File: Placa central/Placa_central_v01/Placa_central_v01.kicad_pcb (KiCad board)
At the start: 2 copper layers, 36 parts, among them J1 Conn_8.4V_PlacaAlimentação, J16 Conn_01x01_Motor1PonteHPCB, J2 Conn_01x02_ArduinoTxRx, J26 Conn_02x08_Odd_Even, J27 Conn_01x01_Motor2PonteHPCB, J28 Conn_01x01_Motor1PCBMotor, J29 Conn_01x01_Motor2PCBMotor, J3 Conn_01x01_ArduinoReset, J37 Conn_01x01_8.4VPonteH, J38 Conn_01x01_5VPonteH, J39 Conn_01x01_GNDPonteH, J4 Conn_GND_PlacaAlimentação, J40 Conn_01x01_Motor1PWM, J41 Conn_01x01_Motor1Dir1, J42 Conn_01x01_Motor1Dir2, J43 Conn_01x01_Motor2Dir1, J44 Conn_01x01_Motor2Dir2, J45 Conn_01x01_Motor2PWM, J48 Conn_01x01_5VEncoderEsq, J49 Conn_01x01_OutputEncoderEsq, J50 Conn_01x01_GNDEncoderEsq, J51 Conn_01x01_5VEncoderDir, J52 Conn_01x01_OutputEncoderDir, J53 Conn_01x01_GNDEncoderDir, SW3 SW_comando1

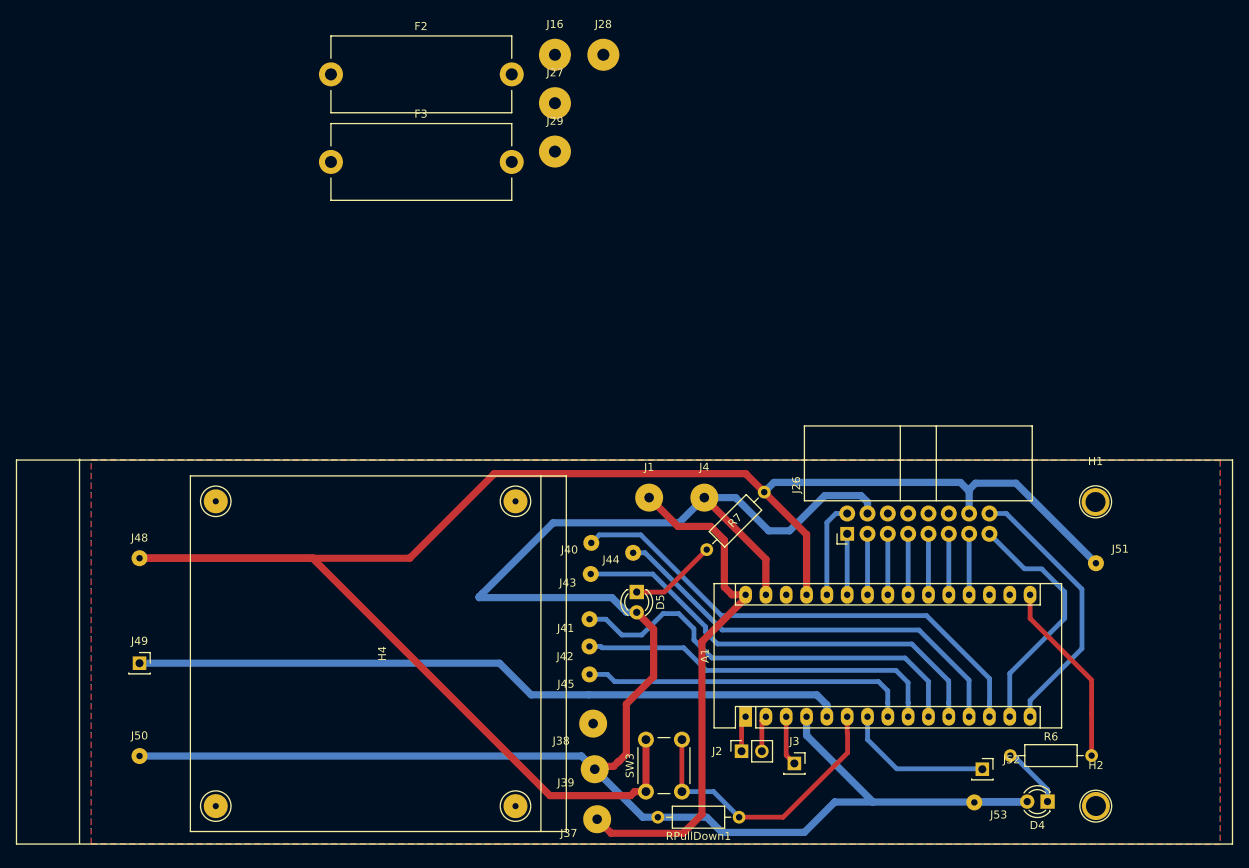
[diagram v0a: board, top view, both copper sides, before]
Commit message: Correção nas pcbs
Nome da placa de encoder desinvertido
Trilhas laterais de GND da placa central mais espaçadas nos cantos
Nome da equipe colocado na placa central
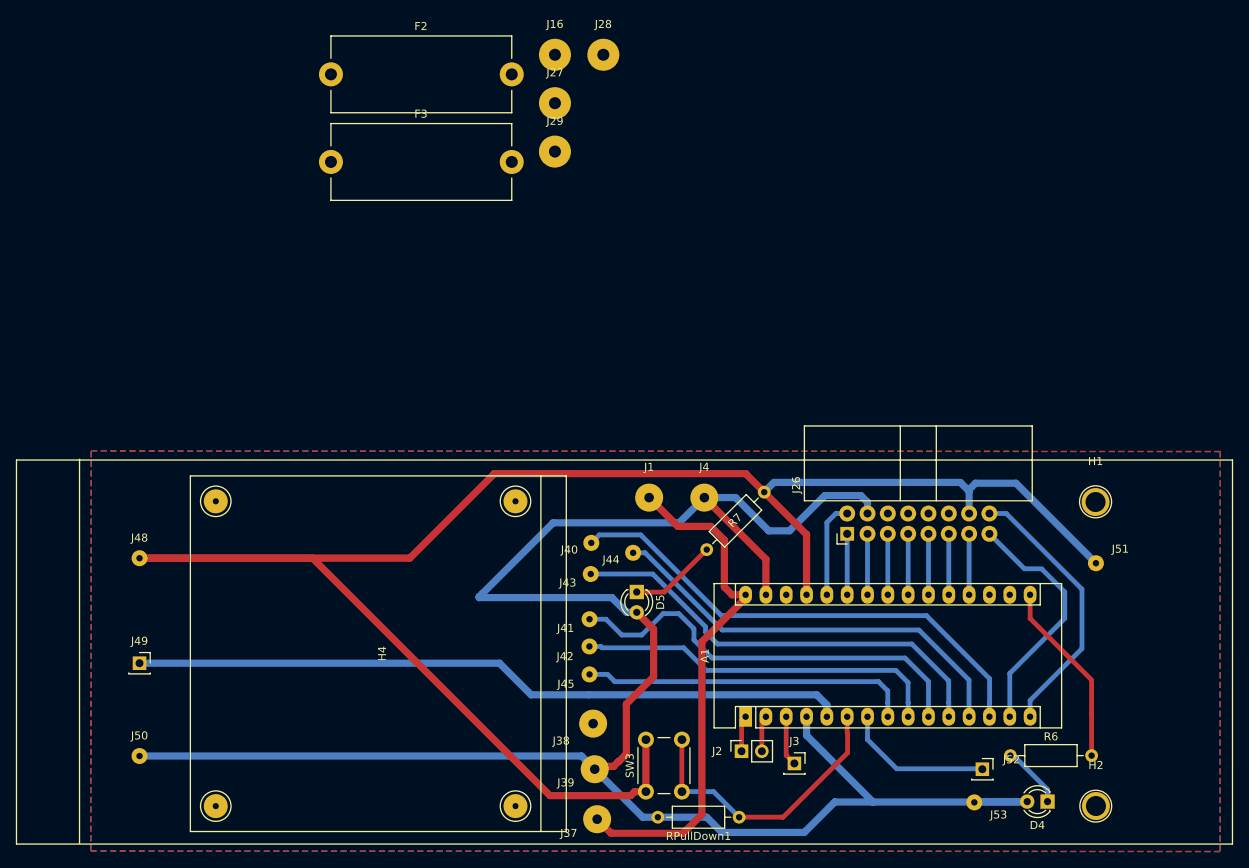
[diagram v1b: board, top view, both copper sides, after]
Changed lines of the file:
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@@
-(kicad_pcb (version 20171130) (host pcbnew 5.1.4-e60b266~84~ubuntu18.04.1)
+(kicad_pcb (version 20171130) (host pcbnew "(5.1.2)-2")
   (general
     (thickness 1.6)
@@
     (visible_elements 7FFFFFFF)
     (pcbplotparams
-      (layerselection 0x000c0_7ffffffe)
+      (layerselection 0x00000_7fffffff)
       (usegerberextensions false)
       (usegerberattributes false)
@@
       (hpglpenspeed 20)
       (hpglpendiameter 15.000000)
-      (psnegative false)
+      (psnegative true)
       (psa4output false)
       (plotreference true)
@@
     (polygon
       (pts
-        (xy 33.95 122.547) (xy 175.1 122.65) (xy 175.1 170.65) (xy 33.95 170.553)
+        (xy 33.95 121.4485) (xy 175.1 121.5515) (xy 175.075 171.5485) (xy 33.925 171.4515)
       )
     )
@@
     (polygon
       (pts
-        (xy 33.95 122.6) (xy 175.1 122.65) (xy 175.1 170.65) (xy 33.95 170.6)
+        (xy 33.95 121.475) (xy 175.1 121.525) (xy 175.075 171.525) (xy 33.925 171.475)
       )
     )

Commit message: Commit complementar ao anterior
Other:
- board text added: "S.L. - ERUS - Pl. CENTRAL"
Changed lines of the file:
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@@
   (general
     (thickness 1.6)
-    (drawings 7)
+    (drawings 9)
     (tracks 190)
     (zones 0)
@@
     (visible_elements 7FFFFFFF)
     (pcbplotparams
-      (layerselection 0x00000_7fffffff)
+      (layerselection 0x00000_fffffffe)
       (usegerberextensions false)
       (usegerberattributes false)
@@
     (pad 1 thru_hole circle (at 0 0) (size 3.5 3.5) (drill 2.49936) (layers *.Cu *.Mask))
   )
+  (gr_text "S.L. - ERUS - Pl. CENTRAL" (at 170.5 147 90) (layer B.Cu)
+    (effects (font (size 1.5 1.5) (thickness 0.375)) (justify mirror))
+  )
+  (gr_text "S.L. - ERUS - Pl. CENTRAL" (at 170.5 147.5 90) (layer F.Cu)
+    (effects (font (size 1.5 1.5) (thickness 0.375)))
+  )
   (gr_line (start 32.5 122.5) (end 32.5 170.5) (layer F.SilkS) (width 0.12))

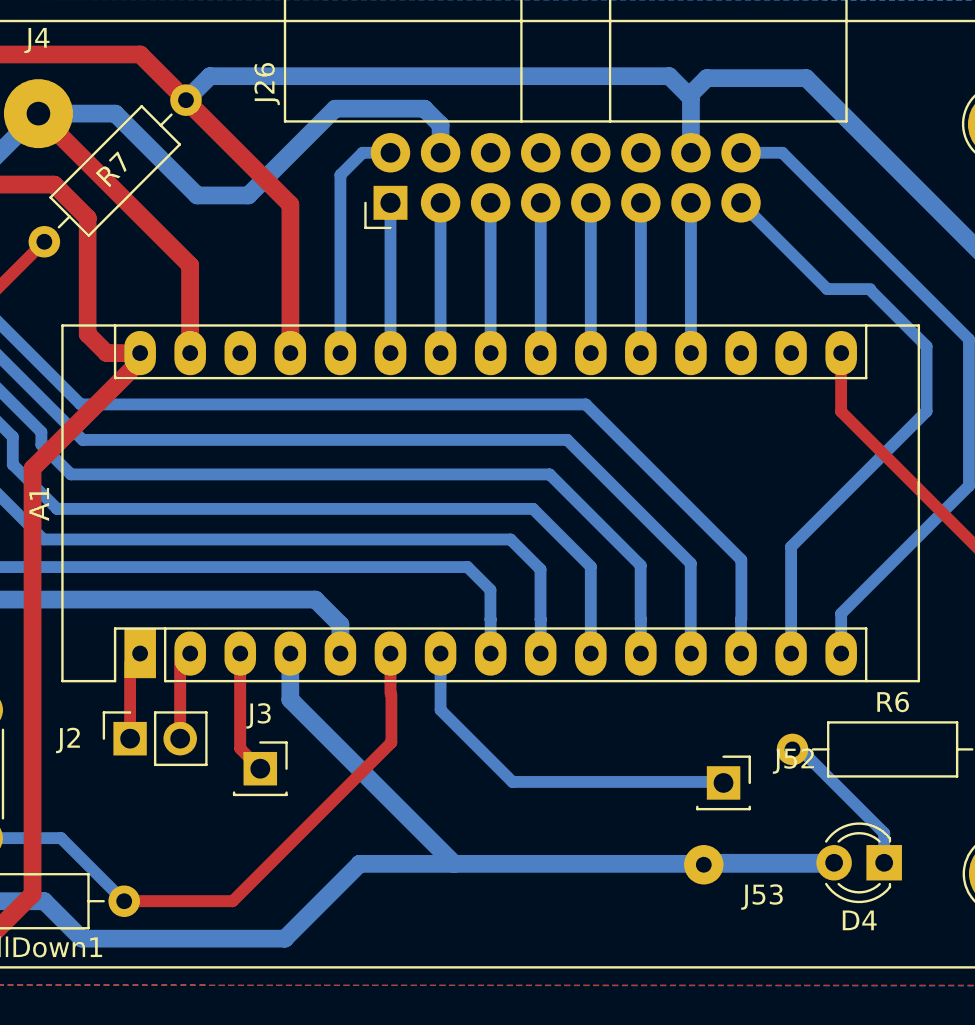
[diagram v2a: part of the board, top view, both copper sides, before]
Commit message: Mudancas criticas na PCB Central, ainda ha pendencias
Foi trocado o pino do botao pelo pino do encoder. Os encoders devem estar obrigatoriamente nos pinos D2 e D3:
Encoder2 para o pino 6 (D3)
Botao1 para o pino 7 (D4);
Aumentadas as dimensoes dos pads conectores do arduino, para mais seguranca ao furar;
Pads do conector modificados para melhor seguranca ao furar;
Clearance da malha de ground aumentada de 0.5 para 0.7
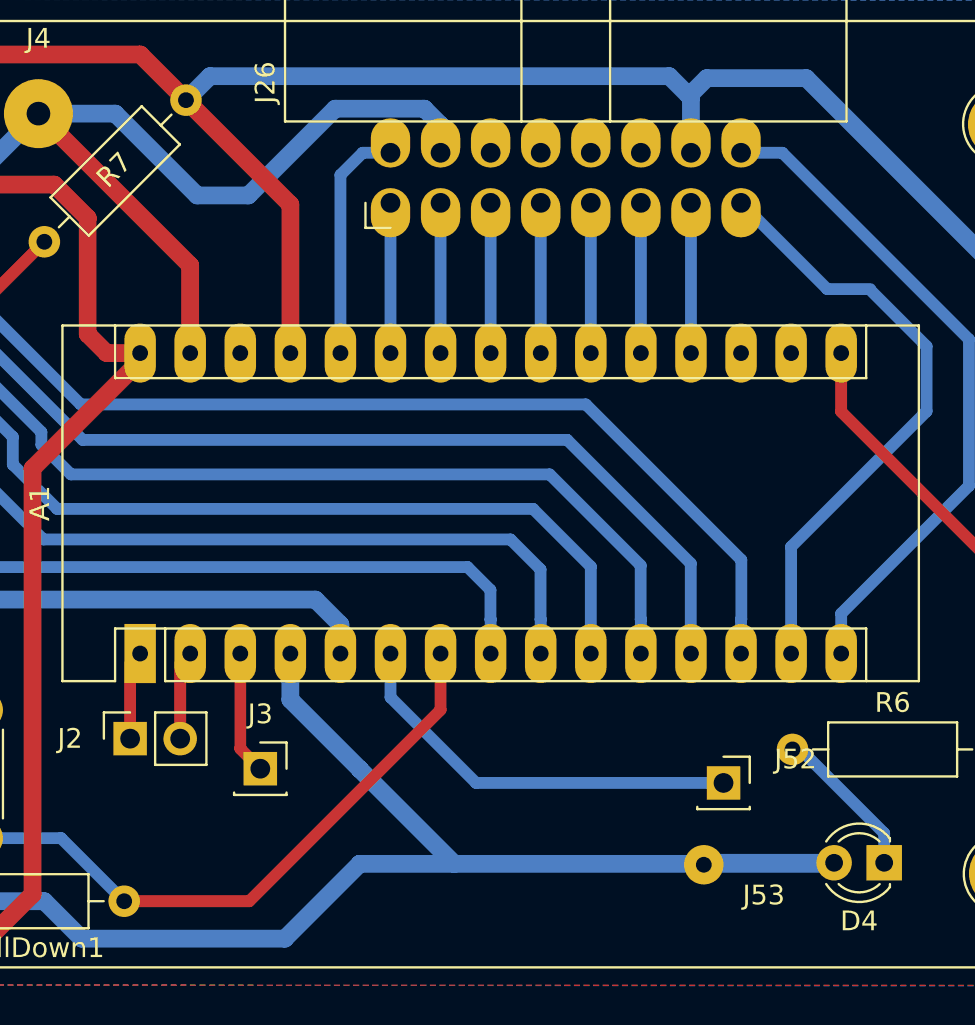
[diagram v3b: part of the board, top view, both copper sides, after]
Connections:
- A1 pad 6: Botao1 -> Encoder2
- A1 pad 7: Encoder2 -> Botao1
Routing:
- net Encoder2: track 18.7 -> 21.2 mm
- net Botao1: track 36.7 -> 37.9 mm

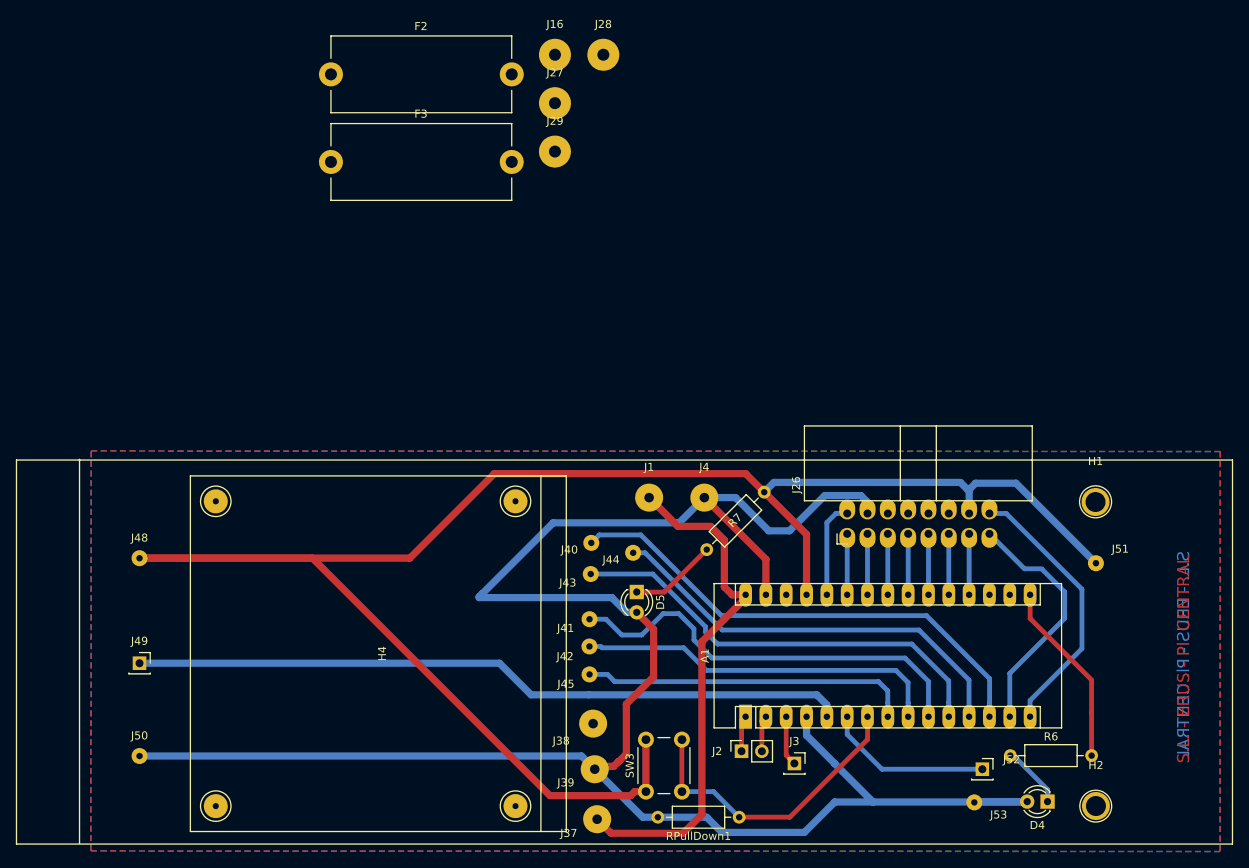
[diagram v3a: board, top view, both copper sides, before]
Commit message: Acertada as placas e os pdfs
Acertada as placas centrais, de alimentação e de conector.
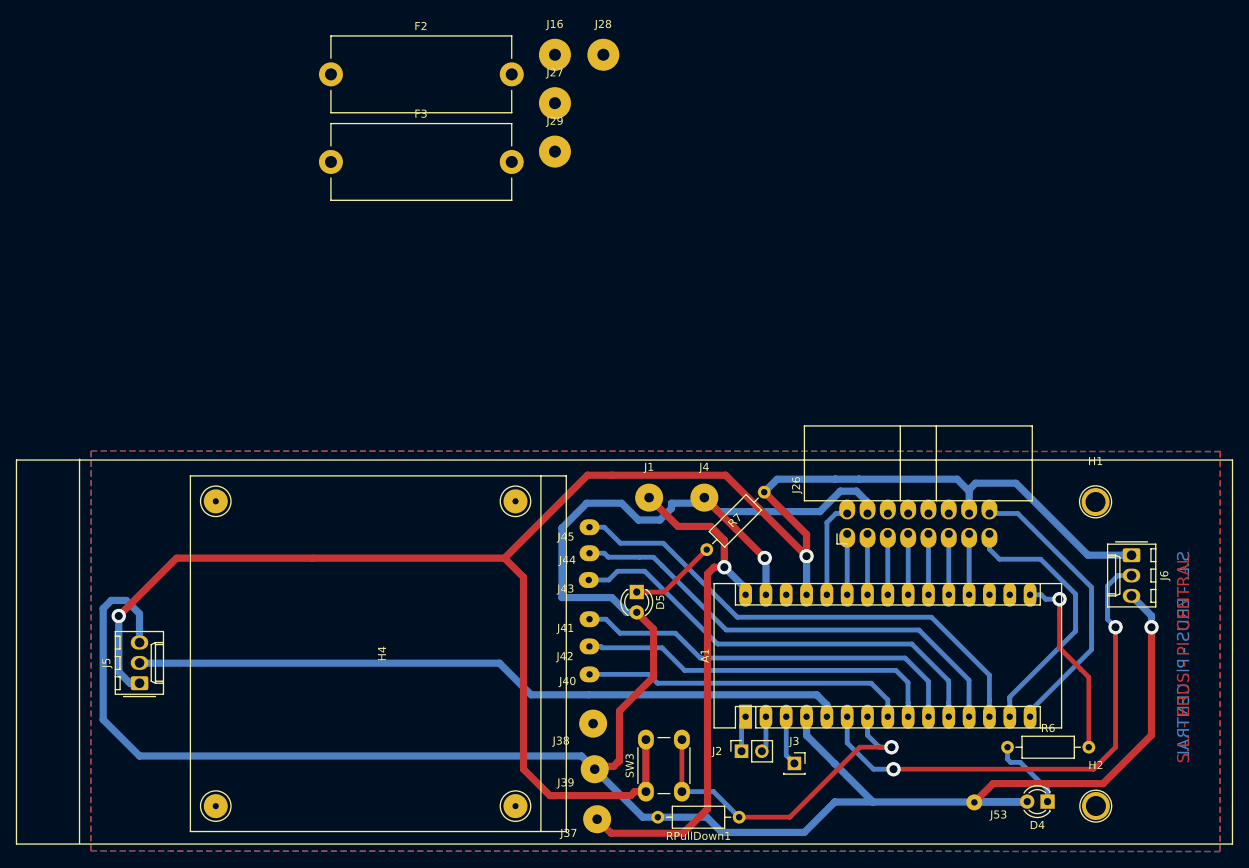
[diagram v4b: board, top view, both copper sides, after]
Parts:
- removed J48: Conn_01x01_5VEncoderEsq, Connector_Wire:SolderWirePad_1x01_Drill0.8mm
- removed J49: Conn_01x01_OutputEncoderEsq, Connector_PinSocket_2.54mm:PinSocket_1x01_P2.54mm_Vertical
- removed J50: Conn_01x01_GNDEncoderEsq, Connector_Wire:SolderWirePad_1x01_Drill0.8mm
- removed J51: Conn_01x01_5VEncoderDir, Connector_Wire:SolderWirePad_1x01_Drill0.8mm
- removed J52: Conn_01x01_OutputEncoderDir, Connector_PinSocket_2.54mm:PinSocket_1x01_P2.54mm_Vertical
- added J5: Conn_01x03_Female, Connector_Molex:Molex_KK-254_AE-6410-03A_1x03_P2.54mm_Vertical, F.Cu at (40.0, 150.5)
- added J6: Conn_01x03_Female, Connector_Molex:Molex_KK-254_AE-6410-03A_1x03_P2.54mm_Vertical, F.Cu at (164.0, 134.5)
- moved J45 18.4 mm to (96.2, 131.0)
- moved J40 16.4 mm to (96.2, 149.4)
- moved J44 5.45 mm to (96.2, 134.2)
- moved R6 1.11 mm to (148.5, 158.5)
- moved J43 0.79 mm to (96.2, 137.6)
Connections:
- A1 pad 13: Motor1PWM -> Motor2PWM
- A1 pad 8: Motor2PWM -> Motor1PWM
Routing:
- net GND: track 256.9 -> 315.5 mm, vias 0 -> 2
- net Encoder2: track 21.2 -> 63.8 mm, vias 0 -> 2
- net Motor1PWM: track 62.7 -> 41.0 mm
- net Motor2PWM: track 41.7 -> 63.2 mm
- net Botao1: track 37.9 -> 44.1 mm, vias 0 -> 1
- net Motor2Dir2: track 53.2 -> 58.6 mm
- net Motor1Dir1: track 53.4 -> 50.3 mm
- net SensorEsq: track 30.7 -> 33.7 mm
- net 5VArduino: track 230.6 -> 227.6 mm, vias 0 -> 2
- net 8.4V: track 65.1 -> 67.1 mm, vias 0 -> 1
- net SensorDir: track 34.1 -> 35.9 mm
- net Net-(D4-Pad1): track 7.91 -> 9.57 mm
- net Rx: track 3.81 -> 4.53 mm
- net LedAzul: track 23.3 -> 24.0 mm, vias 0 -> 1
